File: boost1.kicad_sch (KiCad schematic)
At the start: 18 parts, among them Q1 G1003B-23, U2 LM3478MA

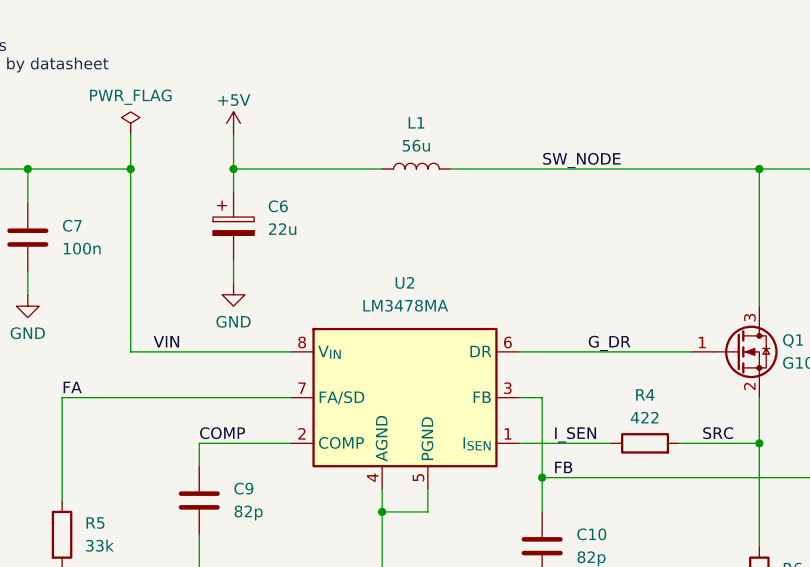
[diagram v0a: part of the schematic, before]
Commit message: Removed 8V boost converter
Now using an isolated 5V power supply module
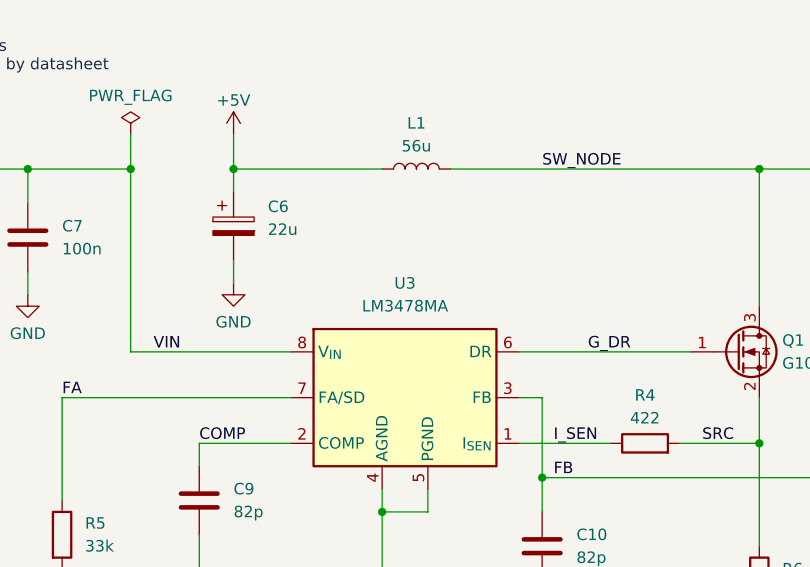
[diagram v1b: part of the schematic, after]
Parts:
- JP2: footprint Connector_PinHeader_2.54mm:PinHeader_1x02_P2.54mm_Vertical_SMD_Pin1Left -> Connector_PinHeader_2.54mm:PinHeader_1x02_P2.54mm_Vertical
- renumbered U2 to U3
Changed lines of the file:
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@@
 		(title "50V Boost Converter")
 		(date "2025-11-27")
+		(rev "1")
 	)
 	(rectangle
@@
 		(on_board yes)
 		(dnp no)
-		(property "Reference" "#PWR032"
+		(property "Reference" "#PWR033"
 			(at 146.05 133.35 0)
 			(effects
@@
 			(project "GP1247AI"
 				(path "/152923e7-b4e9-428d-b807-06741b10ce95/ec69a995-d617-4e33-98ce-41240fe0235f"
-					(reference "#PWR032")
+					(reference "#PWR033")
 					(unit 1)
 				)
@@
 		(on_board yes)
 		(dnp no)
-		(property "Reference" "#PWR034"
+		(property "Reference" "#PWR035"
 			(at 187.96 133.35 0)
 			(effects
@@
 			(project "GP1247AI"
 				(path "/152923e7-b4e9-428d-b807-06741b10ce95/ec69a995-d617-4e33-98ce-41240fe0235f"
-					(reference "#PWR034")
+					(reference "#PWR035")
 					(unit 1)
 				)
@@
 		(on_board yes)
 		(dnp no)
-		(property "Reference" "#PWR035"
+		(property "Reference" "#PWR036"
 			(at 212.09 133.35 0)
 			(effects
@@
 			(project "GP1247AI"
 				(path "/152923e7-b4e9-428d-b807-06741b10ce95/ec69a995-d617-4e33-98ce-41240fe0235f"
-					(reference "#PWR035")
+					(reference "#PWR036")
 					(unit 1)
 				)
@@
 		(on_board yes)
 		(dnp no)
-		(property "Reference" "#PWR030"
+		(property "Reference" "#PWR031"
 			(at 110.49 133.35 0)
 			(effects
@@
 			(project "GP1247AI"
 				(path "/152923e7-b4e9-428d-b807-06741b10ce95/ec69a995-d617-4e33-98ce-41240fe0235f"
-					(reference "#PWR030")
+					(reference "#PWR031")
 					(unit 1)
 				)
@@
 		(on_board yes)
 		(dnp no)
-		(property "Reference" "#PWR028"
+		(property "Reference" "#PWR029"
 			(at 106.68 91.44 0)
 			(effects
@@
 			(project "GP1247AI"
 				(path "/152923e7-b4e9-428d-b807-06741b10ce95/ec69a995-d617-4e33-98ce-41240fe0235f"
-					(reference "#PWR028")
+					(reference "#PWR029")
 					(unit 1)
 				)
@@
 		(on_board yes)
 		(dnp no)
-		(property "Reference" "#PWR026"
+		(property "Reference" "#PWR027"
 			(at 242.57 71.12 0)
 			(effects
@@
 			(project "GP1247AI"
 				(path "/152923e7-b4e9-428d-b807-06741b10ce95/ec69a995-d617-4e33-98ce-41240fe0235f"
-					(reference "#PWR026")
+					(reference "#PWR027")
 					(unit 1)
 				)
@@
 		(on_board yes)
 		(dnp no)
-		(property "Reference" "#PWR027"
+		(property "Reference" "#PWR028"
 			(at 129.54 90.17 0)
 			(effects
@@
 			(project "GP1247AI"
 				(path "/152923e7-b4e9-428d-b807-06741b10ce95/ec69a995-d617-4e33-98ce-41240fe0235f"
-					(reference "#PWR027")
+					(reference "#PWR028")
 					(unit 1)
 				)
@@
 			)
 		)
-		(property "Footprint" "Connector_PinHeader_2.54mm:PinHeader_1x02_P2.54mm_Vertical_SMD_Pin1Left"
+		(property "Footprint" "Connector_PinHeader_2.54mm:PinHeader_1x02_P2.54mm_Vertical"
 			(at 236.22 71.12 0)
 			(effects
@@
 		(on_board yes)
 		(dnp no)
-		(property "Reference" "#PWR031"
+		(property "Reference" "#PWR032"
 			(at 125.73 133.35 0)
 			(effects
@@
 			(project "GP1247AI"
 				(path "/152923e7-b4e9-428d-b807-06741b10ce95/ec69a995-d617-4e33-98ce-41240fe0235f"
-					(reference "#PWR031")
+					(reference "#PWR032")
 					(unit 1)
 				)
@@
 		(on_board yes)
 		(dnp no)
-		(property "Reference" "#PWR024"
+		(property "Reference" "#PWR025"
 			(at 91.44 71.12 0)
 			(effects
@@
 			(project "GP1247AI"
 				(path "/152923e7-b4e9-428d-b807-06741b10ce95/ec69a995-d617-4e33-98ce-41240fe0235f"
-					(reference "#PWR024")
+					(reference "#PWR025")
 					(unit 1)
 				)
@@
 		(on_board yes)
 		(dnp no)
-		(property "Reference" "#PWR025"
+		(property "Reference" "#PWR026"
 			(at 129.54 71.12 0)
 			(effects
@@
 			(project "GP1247AI"
 				(path "/152923e7-b4e9-428d-b807-06741b10ce95/ec69a995-d617-4e33-98ce-41240fe0235f"
-					(reference "#PWR025")
+					(reference "#PWR026")
 					(unit 1)
 				)
@@
 		(on_board yes)
 		(dnp no)
-		(property "Reference" "#PWR029"
+		(property "Reference" "#PWR030"
 			(at 231.14 96.52 0)
 			(effects
@@
 			(project "GP1247AI"
 				(path "/152923e7-b4e9-428d-b807-06741b10ce95/ec69a995-d617-4e33-98ce-41240fe0235f"
-					(reference "#PWR029")
+					(reference "#PWR030")
 					(unit 1)
 				)
@@
 		(on_board yes)
 		(dnp no)
-		(property "Reference" "#PWR033"
+		(property "Reference" "#PWR034"
 			(at 163.83 133.35 0)
 			(effects
@@
 			(project "GP1247AI"
 				(path "/152923e7-b4e9-428d-b807-06741b10ce95/ec69a995-d617-4e33-98ce-41240fe0235f"
-					(reference "#PWR033")
+					(reference "#PWR034")
 					(unit 1)
 				)
@@
 		(on_board yes)
 		(dnp no)
-		(property "Reference" "#FLG08"
+		(property "Reference" "#FLG06"
 			(at 118.11 65.405 0)
 			(effects
@@
 			(project "GP1247AI"
 				(path "/152923e7-b4e9-428d-b807-06741b10ce95/ec69a995-d617-4e33-98ce-41240fe0235f"
-					(reference "#FLG08")
+					(reference "#FLG06")
 					(unit 1)
 				)
@@
 		(dnp no)
 		(fields_autoplaced yes)
-		(property "Reference" "U2"
+		(property "Reference" "U3"
 			(at 148.59 83.82 0)
 			(effects
@@
 			(project "GP1247AI"
 				(path "/152923e7-b4e9-428d-b807-06741b10ce95/ec69a995-d617-4e33-98ce-41240fe0235f"
-					(reference "U2")
+					(reference "U3")
 					(unit 1)
 				)

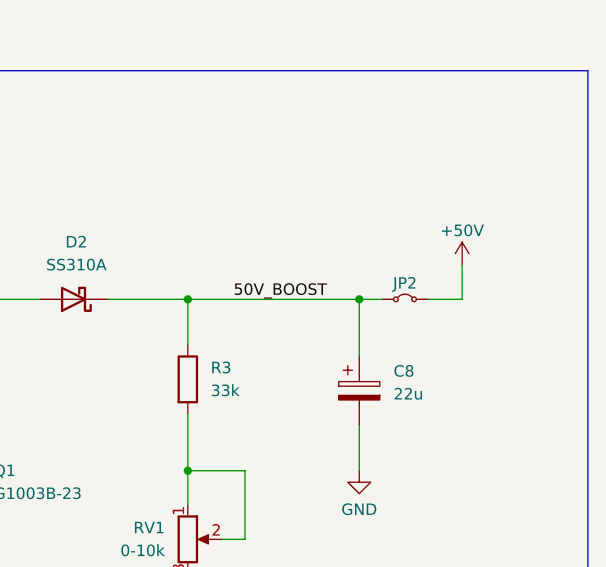
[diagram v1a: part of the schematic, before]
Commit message: Fixed boost2 feedback resistors
Old feedback resistor network made output voltage too high
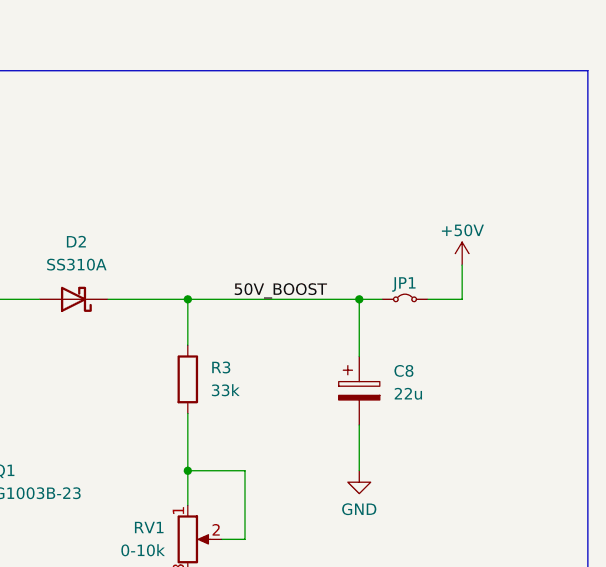
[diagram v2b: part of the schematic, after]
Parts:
- renumbered JP2 to JP1
